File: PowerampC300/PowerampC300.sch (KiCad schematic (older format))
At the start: 111 parts, among them J1 Conn_01x02, J2 Conn_01x02, J3 Conn_01x02, J4 Conn_01x01, J5 Conn_01x01, J6 Conn_01x01, J7 Conn_01x01, J8 Conn_01x02, J9 Conn_Coaxial, Q1 2N5551, Q10 MJE15033, Q11 MJE15032, Q12 MJE15032, Q13 2N5551, Q14 2N5401, Q15 MJE15032, Q16 MJE15033, Q17 MJL3281A, Q18 MJL1302A, Q19 MJL3281A, Q2 2N5551, Q20 MJL1302A, Q21 MJL3281A, Q22 MJL1302A, Q23 MJL3281A, Q24 MJL1302A, Q3 2N5401, Q4 2N5401, Q5 2N5551, Q6 2N5551, Q7 2N5551, Q8 2N5401

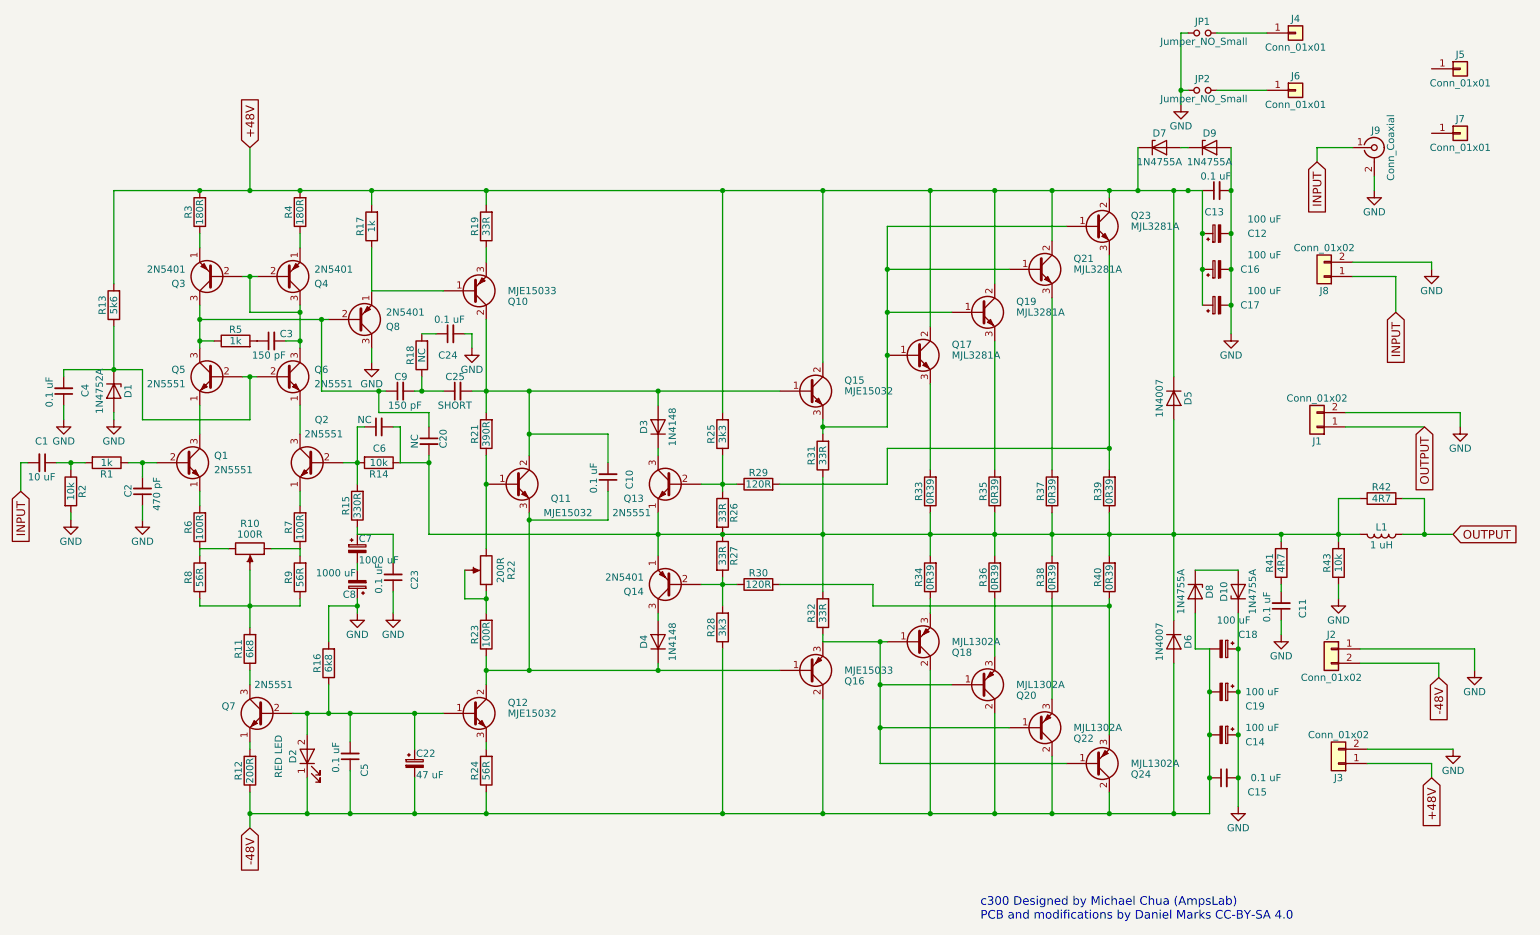
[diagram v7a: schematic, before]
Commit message: Redid star scheme again, added grounding diagram, modified drill template
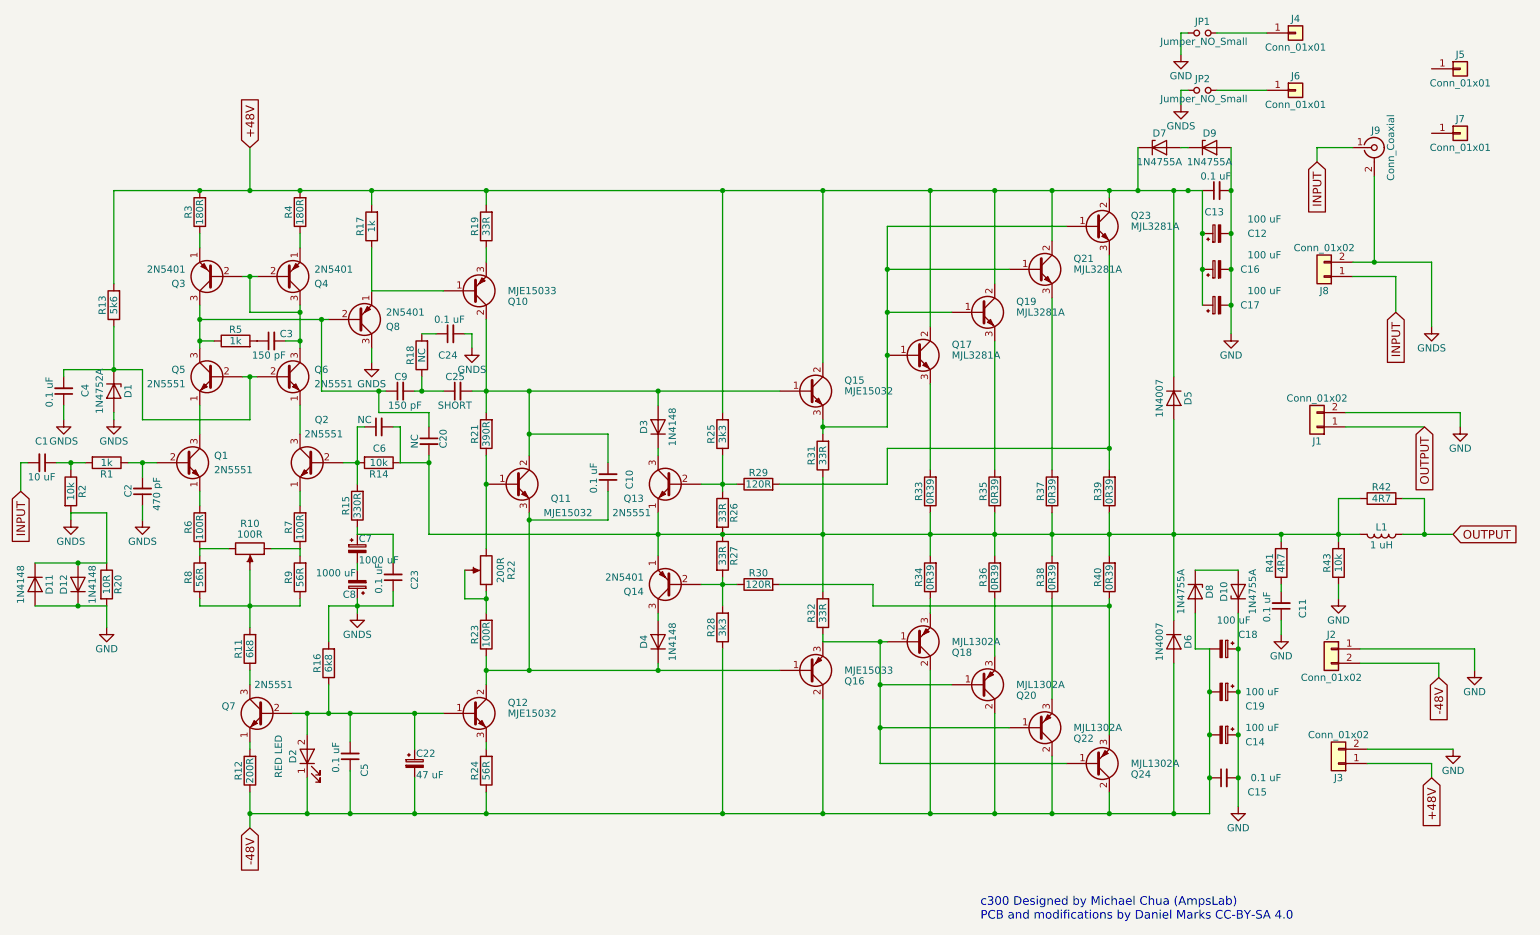
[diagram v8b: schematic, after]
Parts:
- added D11, D12: 1N4148, Diodes_THT:D_DO-35_SOD27_P7.62mm_Horizontal, symbol D
- added R20: 10R, Resistors_THT:R_Axial_DIN0207_L6.3mm_D2.5mm_P7.62mm_Horizontal, symbol R
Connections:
- net GND: now also D11.2 (A), D12.1 (K), R20.2; no longer C2.1, C23.1, C24.2, C4.1, C8.1, D1.2 (A), J8.2 (Pin_2), J9.2 (Ext), JP2.1, Q8.3 (C), R16.2, R2.2
- new net GNDS: C2.1, C23.1, C24.2, C4.1, C8.1, D1.2 (A), D11.1 (K), D12.2 (A), J8.2 (Pin_2), J9.2 (Ext), JP2.1, Q8.3 (C), R16.2, R2.2, R20.1
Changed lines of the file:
@@
-$EndComp
-$Comp
-L GND #PWR2
-U 1 1 5F3B0902
-P 1000 4100
-F 0 "#PWR2" H 1000 3850 50  0001 C CNN
-F 1 "GND" H 1000 3950 50  0000 C CNN
-F 2 "" H 1000 4100 50  0001 C CNN
-F 3 "" H 1000 4100 50  0001 C CNN
-	1    1000 4100
-	1    0    0    -1
 $EndComp
 $Comp
@@
 $EndComp
 $Comp
-L GND #PWR4
+L GND #PWR01
 U 1 1 5F3B09D1
-P 1500 4100
-F 0 "#PWR4" H 1500 3850 50  0001 C CNN
-F 1 "GND" H 1500 3950 50  0000 C CNN
-F 2 "" H 1500 4100 50  0001 C CNN
-F 3 "" H 1500 4100 50  0001 C CNN
-	1    1500 4100
+P 1250 4850
+F 0 "#PWR01" H 1250 4600 50  0001 C CNN
+F 1 "GND" H 1250 4700 50  0000 C CNN
+F 2 "" H 1250 4850 50  0001 C CNN
+F 3 "" H 1250 4850 50  0001 C CNN
+	1    1250 4850
 	1    0    0    -1
 $EndComp
@@
 $EndComp
 $Comp
-L GND #PWR1
-U 1 1 5F3B1EB5
-P 950 3400
-F 0 "#PWR1" H 950 3150 50  0001 C CNN
-F 1 "GND" H 950 3250 50  0000 C CNN
-F 2 "" H 950 3400 50  0001 C CNN
-F 3 "" H 950 3400 50  0001 C CNN
-	1    950  3400
-	1    0    0    -1
-$EndComp
-$Comp
 L D_Zener D1
 U 1 1 5F3B1F13
@@
 $EndComp
 $Comp
-L GND #PWR3
-U 1 1 5F3B1F70
-P 1300 3400
-F 0 "#PWR3" H 1300 3150 50  0001 C CNN
-F 1 "GND" H 1300 3250 50  0000 C CNN
-F 2 "" H 1300 3400 50  0001 C CNN
-F 3 "" H 1300 3400 50  0001 C CNN
-	1    1300 3400
-	1    0    0    -1
-$EndComp
-$Comp
 L R R5
 U 1 1 5F3B2121
@@
 $EndComp
 $Comp
-L GND #PWR5
-U 1 1 5F3B40A9
-P 3000 4750
-F 0 "#PWR5" H 3000 4500 50  0001 C CNN
-F 1 "GND" H 3000 4600 50  0000 C CNN
-F 2 "" H 3000 4750 50  0001 C CNN
-F 3 "" H 3000 4750 50  0001 C CNN
-	1    3000 4750
-	1    0    0    -1
-$EndComp
-$Comp
 L R R15
 U 1 1 5F3B41CE
@@
 $EndComp
 $Comp
-L GND #PWR6
-U 1 1 5F3B638D
-P 3100 3000
-F 0 "#PWR6" H 3100 2750 50  0001 C CNN
-F 1 "GND" H 3100 2850 50  0000 C CNN
-F 2 "" H 3100 3000 50  0001 C CNN
-F 3 "" H 3100 3000 50  0001 C CNN
-	1    3100 3000
-	1    0    0    -1
-$EndComp
-$Comp
 L R R17
 U 1 1 5F3B6489
@@
 $EndComp
 $Comp
-L GND #PWR12
+L GND #PWR02
 U 1 1 5F3C725A
 P 9450 4900
-F 0 "#PWR12" H 9450 4650 50  0001 C CNN
+F 0 "#PWR02" H 9450 4650 50  0001 C CNN
 F 1 "GND" H 9450 4750 50  0000 C CNN
 F 2 "" H 9450 4900 50  0001 C CNN
@@
 $EndComp
 $Comp
-L GND #PWR11
+L GND #PWR03
 U 1 1 5F3C82FF
 P 9150 6100
-F 0 "#PWR11" H 9150 5850 50  0001 C CNN
+F 0 "#PWR03" H 9150 5850 50  0001 C CNN
 F 1 "GND" H 9150 5950 50  0000 C CNN
 F 2 "" H 9150 6100 50  0001 C CNN
@@
 $EndComp
 $Comp
-L GND #PWR10
+L GND #PWR04
 U 1 1 5F3C9FC4
 P 9100 2800
-F 0 "#PWR10" H 9100 2550 50  0001 C CNN
+F 0 "#PWR04" H 9100 2550 50  0001 C CNN
 F 1 "GND" H 9100 2650 50  0000 C CNN
 F 2 "" H 9100 2800 50  0001 C CNN
@@
 OUTPUT
 $Comp
-L GND #PWR17
+L GND #PWR05
 U 1 1 5F3D5C64
 P 10700 3450
-F 0 "#PWR17" H 10700 3200 50  0001 C CNN
+F 0 "#PWR05" H 10700 3200 50  0001 C CNN
 F 1 "GND" H 10700 3300 50  0000 C CNN
 F 2 "" H 10700 3450 50  0001 C CNN
@@
 $EndComp
 $Comp
-L GND #PWR16
+L GND #PWR06
 U 1 1 5F3D7497
 P 10650 5700
-F 0 "#PWR16" H 10650 5450 50  0001 C CNN
+F 0 "#PWR06" H 10650 5450 50  0001 C CNN
 F 1 "GND" H 10650 5550 50  0000 C CNN
 F 2 "" H 10650 5700 50  0001 C CNN
@@
 $EndComp
 $Comp
-L GND #PWR18
+L GND #PWR07
 U 1 1 5F3D76F6
 P 10800 5150
-F 0 "#PWR18" H 10800 4900 50  0001 C CNN
+F 0 "#PWR07" H 10800 4900 50  0001 C CNN
 F 1 "GND" H 10800 5000 50  0000 C CNN
 F 2 "" H 10800 5150 50  0001 C CNN
@@
 $EndComp
 $Comp
-L GND #PWR15
-U 1 1 5F3DED23
-P 10500 2350
-F 0 "#PWR15" H 10500 2100 50  0001 C CNN
-F 1 "GND" H 10500 2200 50  0000 C CNN
-F 2 "" H 10500 2350 50  0001 C CNN
-F 3 "" H 10500 2350 50  0001 C CNN
-	1    10500 2350
-	1    0    0    -1
-$EndComp
-$Comp
 L Conn_Coaxial J9
 U 1 1 5F3DF069
@@
 Text GLabel 9700 1600 3    60   Input ~ 0
 INPUT
-$Comp
-L GND #PWR14
-U 1 1 5F3DF546
-P 10100 1800
-F 0 "#PWR14" H 10100 1550 50  0001 C CNN
-F 1 "GND" H 10100 1650 50  0000 C CNN
-F 2 "" H 10100 1800 50  0001 C CNN
-F 3 "" H 10100 1800 50  0001 C CNN
-	1    10100 1800
-	1    0    0    -1
-$EndComp
 $Comp
 L CP_Small C16
@@
 $EndComp
 $Comp
-L GND #PWR9
-U 1 1 5F401BCA
-P 8750 1200
-F 0 "#PWR9" H 8750 950 50  0001 C CNN
-F 1 "GND" H 8750 1050 50  0000 C CNN
-F 2 "" H 8750 1200 50  0001 C CNN
-F 3 "" H 8750 1200 50  0001 C CNN
-	1    8750 1200
-	1    0    0    -1
-$EndComp
-$Comp
 L TIP41C Q12
 U 1 1 5F4FB282
@@
 $EndComp
 $Comp
-L GND #PWR7
-U 1 1 5F648447
-P 3250 4750
-F 0 "#PWR7" H 3250 4500 50  0001 C CNN
-F 1 "GND" H 3250 4600 50  0000 C CNN
-F 2 "" H 3250 4750 50  0001 C CNN
-F 3 "" H 3250 4750 50  0001 C CNN
-	1    3250 4750
-	1    0    0    -1
-$EndComp
-$Comp
 L R R43
 U 1 1 5F8361D5
@@
 $EndComp
 $Comp
-L GND #PWR13
+L GND #PWR08
 U 1 1 5F83634A
 P 9850 4650
-F 0 "#PWR13" H 9850 4400 50  0001 C CNN
+F 0 "#PWR08" H 9850 4400 50  0001 C CNN
 F 1 "GND" H 9850 4500 50  0000 C CNN
 F 2 "" H 9850 4650 50  0001 C CNN
@@
 $EndComp
 $Comp
-L GND #PWR8
-U 1 1 5F849D07
-P 3800 2900
-F 0 "#PWR8" H 3800 2650 50  0001 C CNN
-F 1 "GND" H 3800 2750 50  0000 C CNN
-F 2 "" H 3800 2900 50  0001 C CNN
-F 3 "" H 3800 2900 50  0001 C CNN
-	1    3800 2900
-	1    0    0    -1
-$EndComp
-$Comp
 L Jumper_NO_Small JP1
 U 1 1 5F85A316
@@
 	10250 2400 9950 2400
 Wire Wire Line
-	10500 2350 10500 2300
-Wire Wire Line
-	10500 2300 9950 2300
-Wire Wire Line
 	9700 1600 9700 1500
 Wire Wire Line
 	9700 1500 9950 1500
 Wire Wire Line
-	10100 1800 10100 1700
+	10100 2300 10100 1700
 Wire Wire Line
 	9100 2350 9100 2350
@@
 Connection ~ 8950 5300
 Wire Wire Line
-	8750 700  8750 1200
-Connection ~ 8750 1100
-Wire Wire Line
 	10800 5000 10800 5150
 Wire Wire Line
@@
 Connection ~ 3400 6150
 Wire Wire Line
-	3250 4750 3250 4600
+	3250 4700 3250 4600
 Wire Wire Line
 	3000 4200 3250 4200
@@
 Connection ~ 3150 3200
 Wire Wire Line
-	2800 4700 3000 4700
+	2800 4700 3250 4700
 Wire Wire Line
 	3300 3700 3300 3450
@@
 	3500 3350 3500 3450
 Connection ~ 3500 3700
+Wire Wire Line
+	10500 2300 10500 2750
+Connection ~ 10100 2300
+Wire Wire Line
+	9950 2300 10500 2300
+$Comp
+L GNDS #PWR09
+U 1 1 5F90B752
+P 1000 4100
+F 0 "#PWR09" H 1000 3850 50  0001 C CNN
+F 1 "GNDS" H 1000 3950 50  0000 C CNN
+F 2 "" H 1000 4100 50  0001 C CNN
+F 3 "" H 1000 4100 50  0001 C CNN
+	1    1000 4100
+	1    0    0    -1
+$EndComp
+$Comp
+L GNDS #PWR010
+U 1 1 5F90C0B2
+P 1500 4100
+F 0 "#PWR010" H 1500 3850 50  0001 C CNN
+F 1 "GNDS" H 1500 3950 50  0000 C CNN
+F 2 "" H 1500 4100 50  0001 C CNN
+F 3 "" H 1500 4100 50  0001 C CNN
+	1    1500 4100
+	1    0    0    -1
+$EndComp
+$Comp
+L GNDS #PWR011
+U 1 1 5F90C20A
+P 3000 4750
+F 0 "#PWR011" H 3000 4500 50  0001 C CNN
+F 1 "GNDS" H 3000 4600 50  0000 C CNN
+F 2 "" H 3000 4750 50  0001 C CNN
+F 3 "" H 3000 4750 50  0001 C CNN
+	1    3000 4750
+	1    0    0    -1
+$EndComp
+$Comp
+L GNDS #PWR012
+U 1 1 5F90CB3D
+P 3800 2900
+F 0 "#PWR012" H 3800 2650 50  0001 C CNN
+F 1 "GNDS" H 3800 2750 50  0000 C CNN
+F 2 "" H 3800 2900 50  0001 C CNN
+F 3 "" H 3800 2900 50  0001 C CNN
+	1    3800 2900
+	1    0    0    -1
+$EndComp
+$Comp
+L GNDS #PWR013
+U 1 1 5F90D661
+P 950 3400
+F 0 "#PWR013" H 950 3150 50  0001 C CNN
+F 1 "GNDS" H 950 3250 50  0000 C CNN
+F 2 "" H 950 3400 50  0001 C CNN
+F 3 "" H 950 3400 50  0001 C CNN
+	1    950  3400
+	1    0    0    -1
+$EndComp
+$Comp
+L GNDS #PWR014
+U 1 1 5F90D829
+P 1300 3400
+F 0 "#PWR014" H 1300 3150 50  0001 C CNN
+F 1 "GNDS" H 1300 3250 50  0000 C CNN
+F 2 "" H 1300 3400 50  0001 C CNN
+F 3 "" H 1300 3400 50  0001 C CNN
+	1    1300 3400
+	1    0    0    -1
+$EndComp
+$Comp
+L R R20
+U 1 1 5F90E1D3
+P 1250 4550
+F 0 "R20" V 1330 4550 50  0000 C CNN
+F 1 "10R" V 1250 4550 50  0000 C CNN
+F 2 "Resistors_THT:R_Axial_DIN0207_L6.3mm_D2.5mm_P7.62mm_Horizontal" V 1180 4550 50  0001 C CNN
+F 3 "" H 1250 4550 50  0001 C CNN
+F 4 "C173010" V 1250 4550 60  0001 C CNN "LCSC"
+	1    1250 4550
+	1    0    0    -1
+$EndComp
+Wire Wire Line
+	1000 4050 1250 4050
+Wire Wire Line
+	1250 4400 1250 4050
+Wire Wire Line
+	1250 4700 1250 4850
+$Comp
+L D D12
+U 1 1 5F90F0CB
+P 1050 4550
+F 0 "D12" H 1050 4650 50  0000 C CNN
+F 1 "1N4148" H 1050 4450 50  0000 C CNN
+F 2 "Diodes_THT:D_DO-35_SOD27_P7.62mm_Horizontal" H 1050 4550 50  0001 C CNN
+F 3 "" H 1050 4550 50  0001 C CNN
+F 4 "C125770" H 1050 4550 60  0001 C CNN "LCSC"
+	1    1050 4550
+	0    -1   -1   0
+$EndComp
+Wire Wire Line
+	750  4400 1250 4400
+Wire Wire Line
+	750  4700 1250 4700
+$Comp
+L D D11
+U 1 1 5F90F6D3
+P 750 4550
+F 0 "D11" H 750 4650 50  0000 C CNN
+F 1 "1N4148" H 750 4450 50  0000 C CNN
+F 2 "Diodes_THT:D_DO-35_SOD27_P7.62mm_Horizontal" H 750 4550 50  0001 C CNN
+F 3 "" H 750 4550 50  0001 C CNN
+F 4 "C125770" H 750 4550 60  0001 C CNN "LCSC"
+	1    750  4550
+	0    1    1    0
+$EndComp
+Connection ~ 1050 4400
+Connection ~ 1050 4700
+$Comp
+L GNDS #PWR015
+U 1 1 5F90FE32
+P 3100 3000
+F 0 "#PWR015" H 3100 2750 50  0001 C CNN
+F 1 "GNDS" H 3100 2850 50  0000 C CNN
+F 2 "" H 3100 3000 50  0001 C CNN
+F 3 "" H 3100 3000 50  0001 C CNN
+	1    3100 3000
+	1    0    0    -1
+$EndComp
+$Comp
+L GNDS #PWR016
+U 1 1 5F910AB2
+P 10500 2750
+F 0 "#PWR016" H 10500 2500 50  0001 C CNN
+F 1 "GNDS" H 10500 2600 50  0000 C CNN
+F 2 "" H 10500 2750 50  0001 C CNN
+F 3 "" H 10500 2750 50  0001 C CNN
+	1    10500 2750
+	1    0    0    -1
+$EndComp
+$Comp
+L GNDS #PWR017
+U 1 1 5F911887
+P 8750 1200
+F 0 "#PWR017" H 8750 950 50  0001 C CNN
+F 1 "GNDS" H 8750 1050 50  0000 C CNN
+F 2 "" H 8750 1200 50  0001 C CNN
+F 3 "" H 8750 1200 50  0001 C CNN
+	1    8750 1200
+	1    0    0    -1
+$EndComp
+Wire Wire Line
+	8750 1100 8750 1200
+$Comp
+L GND #PWR?
+U 1 1 5F912230
+P 8750 850
+F 0 "#PWR?" H 8750 600 50  0001 C CNN
+F 1 "GND" H 8750 700 50  0000 C CNN
+F 2 "" H 8750 850 50  0001 C CNN
+F 3 "" H 8750 850 50  0001 C CNN
+	1    8750 850
+	1    0    0    -1
+$EndComp
+Wire Wire Line
+	8750 700  8750 850
 $EndSCHEMATC
